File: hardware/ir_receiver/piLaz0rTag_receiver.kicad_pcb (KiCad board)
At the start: 2 copper layers, 56.9 x 27.9 mm, 4 parts, among them U1 TSOP4838

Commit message: #9 Add gerber files
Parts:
- moved Output1 46.9 mm to (116.0, 80.0)
- moved U1 39.4 mm to (109.0, 88.0)
- moved LED1 38.6 mm to (107.0, 95.0)
- moved Input1 32.4 mm to (94.0, 80.0)
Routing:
- net Net-(Input1-Pad3): track 93.5 -> 0.00 mm
- net Net-(Input1-Pad1): track 92.7 -> 61.9 mm
- net Net-(Input1-Pad4): track 42.0 -> 22.3 mm
- net Net-(LED1-Pad1): track 25.9 -> 11.0 mm
- net Net-(Input1-Pad5): track 22.9 -> 11.2 mm
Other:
- board size 56.9 x 27.9 mm -> 30 x 30 mm
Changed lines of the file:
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@@
     (links 10)
     (no_connects 0)
-    (area 106.096999 99.492999 163.143001 127.583001)
+    (area 89.924999 69.924999 120.075001 100.075001)
     (thickness 1.6)
     (drawings 4)
-    (tracks 25)
+    (tracks 17)
     (zones 0)
     (modules 4)
@@
   )
   (module Socket_Strips:Socket_Strip_Straight_1x05_Pitch2.54mm (layer F.Cu)
-    (at 115.57 104.14)
+    (at 94 80)
     (descr "Through hole straight socket strip, 1x05, 2.54mm pitch, single row")
     (tags "Through hole socket strip THT 1x05 2.54mm single row")
@@
   )
   (module LEDs:LED_D5.0mm-4 (layer F.Cu)
-    (at 135.89 120.65 180)
+    (at 107 95 180)
     (descr "LED, diameter 5.0mm, 2 pins, diameter 5.0mm, 3 pins, diameter 5.0mm, 4 pins, http://www.kingbright.com/attachments/file/psearch/000/00/00/L-154A4SUREQBFZGEW(Ver.9A).pdf")
     (tags "LED diameter 5.0mm 2 pins diameter 5.0mm 3 pins diameter 5.0mm 4 pins")
@@
   )
   (module Socket_Strips:Socket_Strip_Straight_1x05_Pitch2.54mm (layer F.Cu)
-    (at 156.21 104.14)
+    (at 116 80)
     (descr "Through hole straight socket strip, 1x05, 2.54mm pitch, single row")
     (tags "Through hole socket strip THT 1x05 2.54mm single row")
@@
   )
   (module Opto-Devices:IRReceiver_Vishay_MOLD-3pin (layer F.Cu)
-    (at 142.24 109.22 90)
+    (at 109 88 90)
     (descr "IR Receiver Vishay TSOP-xxxx, MOLD package")
     (tags "IR Receiver Vishay TSOP-xxxx MOLD")
@@
       (net 1 "Net-(Input1-Pad1)"))
   )
-  (gr_line (start 106.172 99.568) (end 163.068 99.568) (angle 90) (layer Edge.Cuts) (width 0.15))
-  (gr_line (start 106.172 127.508) (end 106.172 99.568) (angle 90) (layer Edge.Cuts) (width 0.15))
-  (gr_line (start 163.068 127.508) (end 106.172 127.508) (angle 90) (layer Edge.Cuts) (width 0.15))
-  (gr_line (start 163.068 99.568) (end 163.068 127.508) (angle 90) (layer Edge.Cuts) (width 0.15))
-  (segment (start 115.57 104.14) (end 111.76 104.14) (width 0.25) (layer B.Cu) (net 1))
-  (segment (start 133.35 125.73) (end 133.35 120.65) (width 0.25) (layer B.Cu) (net 1))
-  (segment (start 111.76 125.73) (end 133.35 125.73) (width 0.25) (layer B.Cu) (net 1))
-  (segment (start 111.76 124.46) (end 111.76 125.73) (width 0.25) (layer B.Cu) (net 1))
-  (segment (start 111.76 104.14) (end 111.76 124.46) (width 0.25) (layer B.Cu) (net 1))
-  (segment (start 115.57 104.14) (end 142.24 104.14) (width 0.25) (layer B.Cu) (net 1))
-  (segment (start 142.24 104.14) (end 156.21 104.14) (width 0.25) (layer B.Cu) (net 1))
-  (segment (start 156.21 109.22) (end 158.75 109.22) (width 0.25) (layer B.Cu) (net 3))
-  (segment (start 134.62 125.73) (end 134.62 120.65) (width 0.25) (layer B.Cu) (net 3))
-  (segment (start 160.02 125.73) (end 134.62 125.73) (width 0.25) (layer B.Cu) (net 3))
-  (segment (start 160.02 109.22) (end 160.02 125.73) (width 0.25) (layer B.Cu) (net 3))
-  (segment (start 158.75 109.22) (end 160.02 109.22) (width 0.25) (layer B.Cu) (net 3))
-  (segment (start 115.57 109.22) (end 139.7 109.22) (width 0.25) (layer B.Cu) (net 3))
-  (segment (start 139.7 109.22) (end 142.24 106.68) (width 0.25) (layer B.Cu) (net 3))
-  (segment (start 142.24 106.68) (end 153.67 106.68) (width 0.25) (layer B.Cu) (net 3))
-  (segment (start 153.67 106.68) (end 156.21 109.22) (width 0.25) (layer B.Cu) (net 3))
-  (segment (start 142.24 109.22) (end 151.13 111.76) (width 0.25) (layer B.Cu) (net 4))
-  (segment (start 151.13 111.76) (end 156.21 111.76) (width 0.25) (layer B.Cu) (net 4))
-  (segment (start 115.57 111.76) (end 139.7 111.76) (width 0.25) (layer B.Cu) (net 4))
-  (segment (start 139.7 111.76) (end 142.24 109.22) (width 0.25) (layer B.Cu) (net 4))
-  (segment (start 115.57 114.3) (end 115.57 120.65) (width 0.25) (layer B.Cu) (net 5))
-  (segment (start 115.57 120.65) (end 132.08 120.65) (width 0.25) (layer B.Cu) (net 5))
-  (segment (start 135.89 120.65) (end 154.94 120.65) (width 0.25) (layer B.Cu) (net 7))
-  (segment (start 156.21 119.38) (end 156.21 114.3) (width 0.25) (layer B.Cu) (net 7))
-  (segment (start 154.94 120.65) (end 156.21 119.38) (width 0.25) (layer B.Cu) (net 7))
+  (gr_line (start 120 100) (end 90 100) (angle 90) (layer Edge.Cuts) (width 0.15))
+  (gr_line (start 120 70) (end 120 100) (angle 90) (layer Edge.Cuts) (width 0.15))
+  (gr_line (start 90 70) (end 120 70) (angle 90) (layer Edge.Cuts) (width 0.15))
+  (gr_line (start 90 100) (end 90 70) (angle 90) (layer Edge.Cuts) (width 0.15))
+  (segment (start 104.46 95) (end 104.46 97.96) (width 0.25) (layer B.Cu) (net 1) (status 400000))
+  (segment (start 118.5 80) (end 116 80) (width 0.25) (layer B.Cu) (net 1) (status 800000))
+  (segment (start 118.5 98) (end 118.5 80) (width 0.25) (layer B.Cu) (net 1))
+  (segment (start 104.5 98) (end 118.5 98) (width 0.25) (layer B.Cu) (net 1))
+  (segment (start 104.46 97.96) (end 104.5 98) (width 0.25) (layer B.Cu) (net 1))
+  (segment (start 116 80) (end 111.92 80) (width 0.25) (layer B.Cu) (net 1))
+  (segment (start 111.92 80) (end 109 82.92) (width 0.25) (layer B.Cu) (net 1))
+  (segment (start 94 80) (end 106.08 80) (width 0.25) (layer B.Cu) (net 1))
+  (segment (start 106.08 80) (end 109 82.92) (width 0.25) (layer B.Cu) (net 1))
+  (segment (start 109 88) (end 115.62 88) (width 0.25) (layer B.Cu) (net 4))
+  (segment (start 115.62 88) (end 116 87.62) (width 0.25) (layer B.Cu) (net 4))
+  (segment (start 94 87.62) (end 108.62 87.62) (width 0.25) (layer B.Cu) (net 4))
+  (segment (start 108.62 87.62) (end 109 88) (width 0.25) (layer B.Cu) (net 4))
+  (segment (start 103.19 95) (end 98.84 95) (width 0.25) (layer B.Cu) (net 5))
+  (segment (start 98.84 95) (end 94 90.16) (width 0.25) (layer B.Cu) (net 5))
+  (segment (start 107 95) (end 111.16 95) (width 0.25) (layer B.Cu) (net 7))
+  (segment (start 111.16 95) (end 116 90.16) (width 0.25) (layer B.Cu) (net 7))
   (zone (net 3) (net_name "Net-(Input1-Pad3)") (layer B.Cu) (hatch edge 0.508)
     (connect_pads (clearance 0.508))
@@
     (polygon
       (pts
-        (xy 106.68 100.33) (xy 106.68 127) (xy 162.56 127) (xy 162.56 100.33)
+        (xy 90 70) (xy 120 70) (xy 120 100) (xy 90 100)
       )
     )

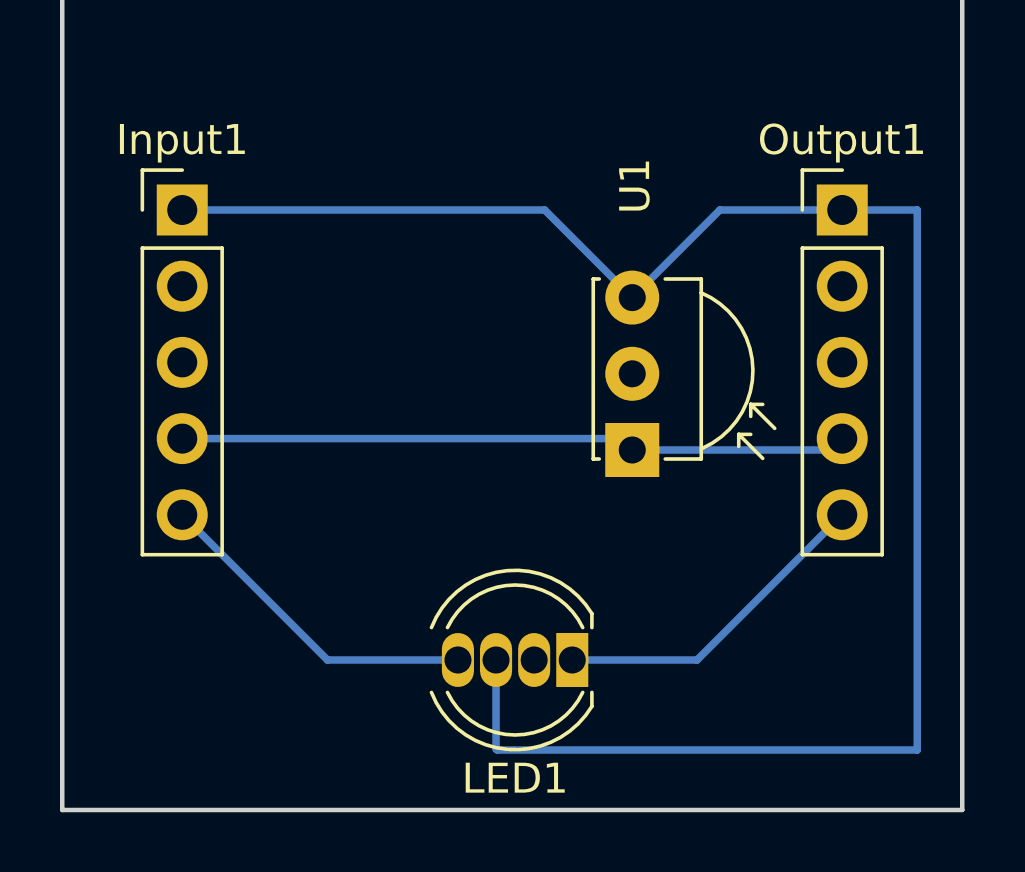
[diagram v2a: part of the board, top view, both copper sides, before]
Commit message: Some rework on the ir receiver pcb
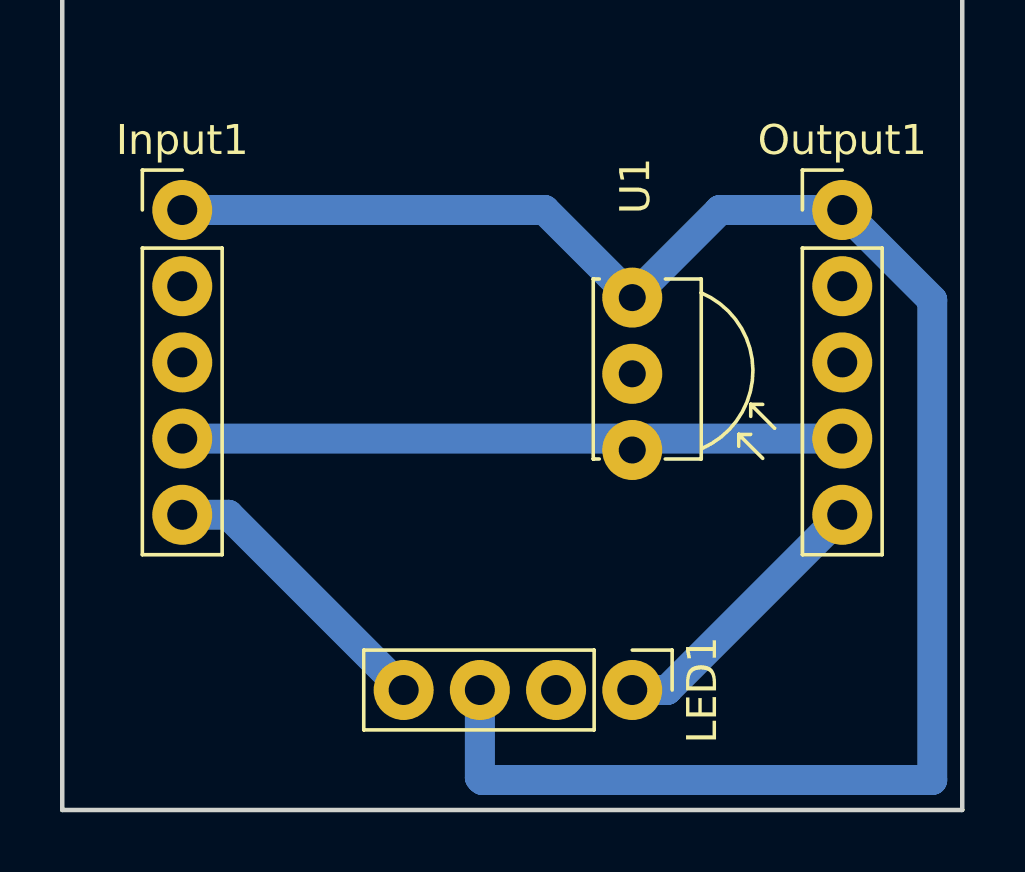
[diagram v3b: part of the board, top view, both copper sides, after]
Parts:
- LED1: footprint LEDs:LED_D5.0mm-4 -> Socket_Strips:Socket_Strip_Straight_1x04_Pitch2.54mm
- moved LED1 2.24 mm to (109.0, 96.0), turned to 270 degrees
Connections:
- Input1 pad 2: Net-(Input1-Pad2) -> (no net)
- Output1 pad 2: Net-(Output1-Pad2) -> (no net)
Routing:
- net Net-(LED1-Pad1): track 11.0 -> 9.42 mm
- net Net-(Input1-Pad5): track 11.2 -> 9.80 mm
- net Net-(Input1-Pad4): track 22.3 -> 23.4 mm
- net Net-(Input1-Pad1): track 61.9 -> 62.7 mm
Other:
- net class Default: trace_width 0.25 -> 1

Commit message: #9 Ir Receiver
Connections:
- Input1 pad 2: (no net) -> Net-(Input1-Pad2)
- Output1 pad 2: (no net) -> Net-(Output1-Pad2)
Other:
- net class Default: clearance 0.2 -> 0.5
- rule trace_clearance: 0.2 -> 0.5
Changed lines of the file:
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@@
     (zones 0)
     (modules 4)
-    (nets 6)
+    (nets 8)
   )
   (page A4)
@@
   (setup
     (last_trace_width 1)
-    (trace_clearance 0.2)
-    (zone_clearance 0.508)
+    (trace_clearance 0.5)
+    (zone_clearance 0.6)
     (zone_45_only no)
     (trace_min 0.2)
@@
     (mod_text_width 0.15)
     (pad_size 2 2)
-    (pad_drill 0.9)
+    (pad_drill 0.8)
     (pad_to_mask_clearance 0.2)
     (aux_axis_origin 0 0)
     (visible_elements FFFFFF7F)
     (pcbplotparams
-      (layerselection 0x00030_80000001)
+      (layerselection 0x00000_80000000)
       (usegerberextensions false)
       (excludeedgelayer true)
@@
   (net 4 "Net-(Input1-Pad5)")
   (net 5 "Net-(LED1-Pad1)")
+  (net 6 "Net-(Input1-Pad2)")
+  (net 7 "Net-(Output1-Pad2)")
   (net_class Default "This is the default net class."
-    (clearance 0.2)
+    (clearance 0.5)
     (trace_width 1)
     (via_dia 0.6)
@@
     (uvia_drill 0.1)
     (add_net "Net-(Input1-Pad1)")
+    (add_net "Net-(Input1-Pad2)")
     (add_net "Net-(Input1-Pad3)")
     (add_net "Net-(Input1-Pad4)")
     (add_net "Net-(Input1-Pad5)")
     (add_net "Net-(LED1-Pad1)")
+    (add_net "Net-(Output1-Pad2)")
   )
   (module Socket_Strips:Socket_Strip_Straight_1x05_Pitch2.54mm (layer F.Cu)
@@
       (effects (font (size 1 1) (thickness 0.15)))
     )
-    (pad 1 thru_hole circle (at 0 0) (size 2 2) (drill 1) (layers *.Cu *.Mask)
-      (net 1 "Net-(Input1-Pad1)"))
-    (pad 2 thru_hole circle (at 0 2.54) (size 2 2) (drill 1) (layers *.Cu *.Mask))
-    (pad 3 thru_hole circle (at 0 5.08) (size 2 2) (drill 1) (layers *.Cu *.Mask)
-      (net 2 "Net-(Input1-Pad3)"))
-    (pad 4 thru_hole circle (at 0 7.62) (size 2 2) (drill 1) (layers *.Cu *.Mask)
+    (pad 1 thru_hole circle (at 0 0) (size 2 2) (drill 0.8) (layers *.Cu *.Mask)
+      (net 1 "Net-(Input1-Pad1)"))
+    (pad 2 thru_hole circle (at 0 2.54) (size 2 2) (drill 0.8) (layers *.Cu *.Mask)
+      (net 6 "Net-(Input1-Pad2)"))
+    (pad 3 thru_hole circle (at 0 5.08) (size 2 2) (drill 0.8) (layers *.Cu *.Mask)
+      (net 2 "Net-(Input1-Pad3)"))
+    (pad 4 thru_hole circle (at 0 7.62) (size 2 2) (drill 0.8) (layers *.Cu *.Mask)
       (net 3 "Net-(Input1-Pad4)"))
-    (pad 5 thru_hole circle (at 0 10.16) (size 2 2) (drill 1) (layers *.Cu *.Mask)
+    (pad 5 thru_hole circle (at 0 10.16) (size 2 2) (drill 0.8) (layers *.Cu *.Mask)
       (net 4 "Net-(Input1-Pad5)"))
     (model ${KISYS3DMOD}/Socket_Strips.3dshapes/Socket_Strip_Straight_1x05_Pitch2.54mm.wrl
@@
       (effects (font (size 1 1) (thickness 0.15)))
     )
-    (pad 1 thru_hole circle (at 0 0) (size 2 2) (drill 1) (layers *.Cu *.Mask)
-      (net 1 "Net-(Input1-Pad1)"))
-    (pad 2 thru_hole circle (at 0 2.54) (size 2 2) (drill 1) (layers *.Cu *.Mask))
-    (pad 3 thru_hole circle (at 0 5.08) (size 2 2) (drill 1) (layers *.Cu *.Mask)
-      (net 2 "Net-(Input1-Pad3)"))
-    (pad 4 thru_hole circle (at 0 7.62) (size 2 2) (drill 1) (layers *.Cu *.Mask)
+    (pad 1 thru_hole circle (at 0 0) (size 2 2) (drill 0.8) (layers *.Cu *.Mask)
+      (net 1 "Net-(Input1-Pad1)"))
+    (pad 2 thru_hole circle (at 0 2.54) (size 2 2) (drill 0.8) (layers *.Cu *.Mask)
+      (net 7 "Net-(Output1-Pad2)"))
+    (pad 3 thru_hole circle (at 0 5.08) (size 2 2) (drill 0.8) (layers *.Cu *.Mask)
+      (net 2 "Net-(Input1-Pad3)"))
+    (pad 4 thru_hole circle (at 0 7.62) (size 2 2) (drill 0.8) (layers *.Cu *.Mask)
       (net 3 "Net-(Input1-Pad4)"))
-    (pad 5 thru_hole circle (at 0 10.16) (size 2 2) (drill 1) (layers *.Cu *.Mask)
+    (pad 5 thru_hole circle (at 0 10.16) (size 2 2) (drill 0.8) (layers *.Cu *.Mask)
       (net 5 "Net-(LED1-Pad1)"))
     (model ${KISYS3DMOD}/Socket_Strips.3dshapes/Socket_Strip_Straight_1x05_Pitch2.54mm.wrl
@@
     (fp_arc (start 2.64 1.2) (end 5.24 2.3) (angle 133) (layer F.SilkS) (width 0.12))
     (fp_arc (start 2.64 1.15) (end 5.14 2.25) (angle 132) (layer F.Fab) (width 0.1))
-    (pad 1 thru_hole circle (at 0 0 90) (size 2 2) (drill 0.9) (layers *.Cu *.Mask)
+    (pad 1 thru_hole circle (at 0 0 90) (size 2 2) (drill 0.8) (layers *.Cu *.Mask)
       (net 3 "Net-(Input1-Pad4)"))
-    (pad 2 thru_hole circle (at 2.54 0 90) (size 2 2) (drill 0.9) (layers *.Cu *.Mask)
-      (net 2 "Net-(Input1-Pad3)"))
-    (pad 3 thru_hole circle (at 5.08 0 90) (size 2 2) (drill 0.9) (layers *.Cu *.Mask)
+    (pad 2 thru_hole circle (at 2.54 0 90) (size 2 2) (drill 0.8) (layers *.Cu *.Mask)
+      (net 2 "Net-(Input1-Pad3)"))
+    (pad 3 thru_hole circle (at 5.08 0 90) (size 2 2) (drill 0.8) (layers *.Cu *.Mask)
       (net 1 "Net-(Input1-Pad1)"))
   )
@@
       (effects (font (size 1 1) (thickness 0.15)))
     )
-    (pad 1 thru_hole circle (at 0 0 270) (size 2 2) (drill 1) (layers *.Cu *.Mask)
+    (pad 1 thru_hole circle (at 0 0 270) (size 2 2) (drill 0.8) (layers *.Cu *.Mask)
       (net 5 "Net-(LED1-Pad1)"))
-    (pad 2 thru_hole circle (at 0 2.54 270) (size 2 2) (drill 1) (layers *.Cu *.Mask)
-      (net 2 "Net-(Input1-Pad3)"))
-    (pad 3 thru_hole circle (at 0 5.08 270) (size 2 2) (drill 1) (layers *.Cu *.Mask)
-      (net 1 "Net-(Input1-Pad1)"))
-    (pad 4 thru_hole circle (at 0 7.62 270) (size 2 2) (drill 1) (layers *.Cu *.Mask)
+    (pad 2 thru_hole circle (at 0 2.54 270) (size 2 2) (drill 0.8) (layers *.Cu *.Mask)
+      (net 2 "Net-(Input1-Pad3)"))
+    (pad 3 thru_hole circle (at 0 5.08 270) (size 2 2) (drill 0.8) (layers *.Cu *.Mask)
+      (net 1 "Net-(Input1-Pad1)"))
+    (pad 4 thru_hole circle (at 0 7.62 270) (size 2 2) (drill 0.8) (layers *.Cu *.Mask)
       (net 4 "Net-(Input1-Pad5)"))
     (model ${KISYS3DMOD}/Socket_Strips.3dshapes/Socket_Strip_Straight_1x04_Pitch2.54mm.wrl
@@
   (segment (start 103.92 98.92) (end 104 99) (width 1) (layer B.Cu) (net 1))
   (segment (start 104 99) (end 119 99) (width 1) (layer B.Cu) (net 1))
-  (segment (start 103.92 96) (end 103.92 98.92) (width 1) (layer B.Cu) (net 1) (status 400000))
-  (segment (start 119 83) (end 116 80) (width 1) (layer B.Cu) (net 1) (status 800000))
+  (segment (start 103.92 96) (end 103.92 98.92) (width 1) (layer B.Cu) (net 1))
+  (segment (start 119 83) (end 116 80) (width 1) (layer B.Cu) (net 1))
   (segment (start 116 80) (end 111.92 80) (width 1) (layer B.Cu) (net 1))
   (segment (start 111.92 80) (end 109 82.92) (width 1) (layer B.Cu) (net 1))
@@
   (segment (start 110.16 96) (end 116 90.16) (width 1) (layer B.Cu) (net 5))
   (zone (net 2) (net_name "Net-(Input1-Pad3)") (layer B.Cu) (hatch edge 0.508)
-    (connect_pads (clearance 0.508))
+    (connect_pads yes (clearance 0.6))
     (min_thickness 0.254)
-    (fill yes (arc_segments 16) (thermal_gap 0.508) (thermal_bridge_width 0.508))
+    (fill yes (mode segment) (arc_segments 16) (thermal_gap 0.6) (thermal_bridge_width 1))
     (polygon
       (pts

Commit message: Some minor changes on the receiver mainboard
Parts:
- removed U1: TSOP4838, Opto-Devices:IRReceiver_Vishay_MOLD-3pin
- added IR_REC1: TSOP4838, Opto-Devices:IRReceiver_Vishay_MOLD-3pin, F.Cu at (109.4, 87.4)
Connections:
- net Net-(Input1-Pad1) renamed +5V
- net Net-(Input1-Pad4) renamed /IR_DATA
- net Net-(Input1-Pad5) renamed /LED_DIN
- net Net-(LED1-Pad1) renamed /LED_DOUT
- Input1 pad 2: Net-(Input1-Pad2) -> GND
- Input1 pad 3: Net-(Input1-Pad3) -> GND
- LED1 pad 2: Net-(Input1-Pad3) -> GND
- Output1 pad 2: Net-(Output1-Pad2) -> GND
- Output1 pad 3: Net-(Input1-Pad3) -> GND
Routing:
- net /IR_DATA: track 23.4 -> 22.7 mm
- added copper zone on B.Cu, net GND
- removed copper zone on B.Cu, net Net-(Input1-Pad3)
